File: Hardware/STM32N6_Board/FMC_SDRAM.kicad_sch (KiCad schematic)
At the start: 15 parts, among them U11 IS42S16800F-7BL

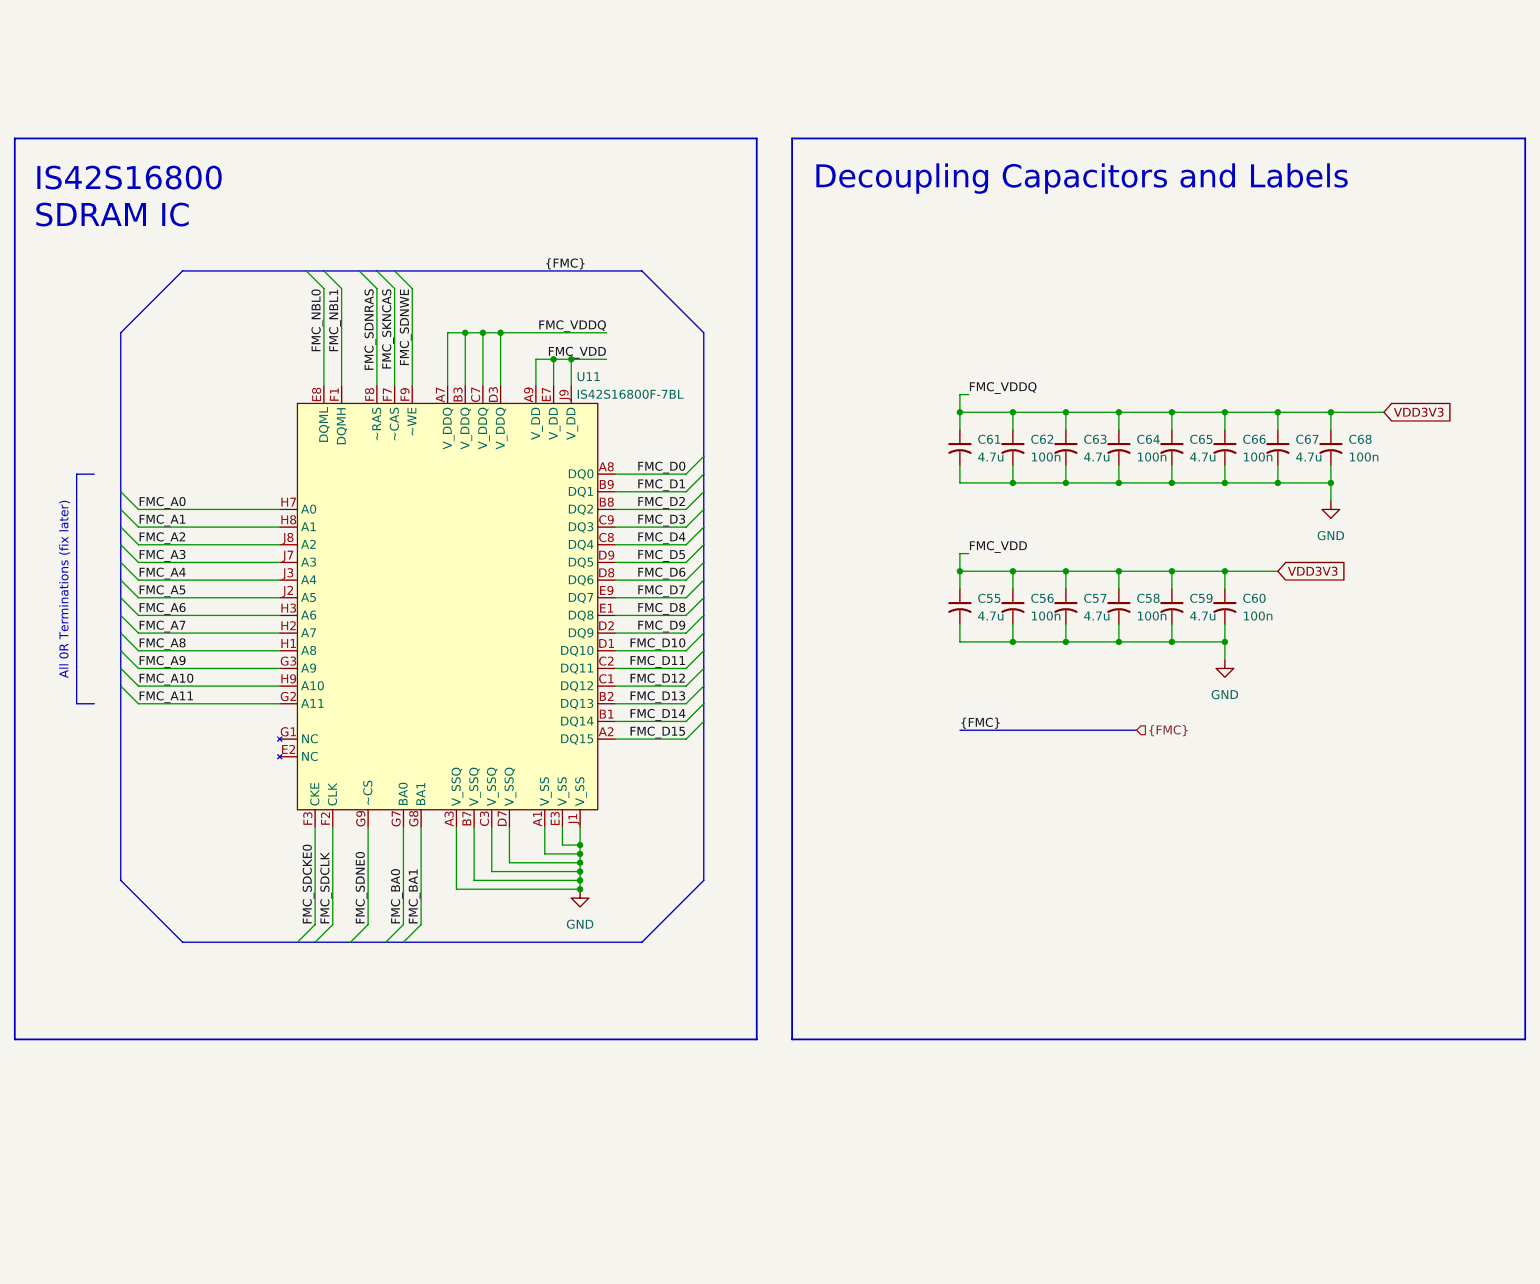
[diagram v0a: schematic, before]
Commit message: Completed the IS42S SDRAM routing. Lord have mercy
- Routing is complete (somewhat)
- Spacing between traces is 0.5mm, address and data lines 0.1565mm wide
- 0.1565mm should maintain ~50 Ohms impedance.
- STILL NEED TO DO:
  - Length matching. Datasheet + STM App Note says +-10mm
  - 10nF stitching caps along vias, for return currents
- Remind me to *never* use a 4-layer board for something like this
  again. D:
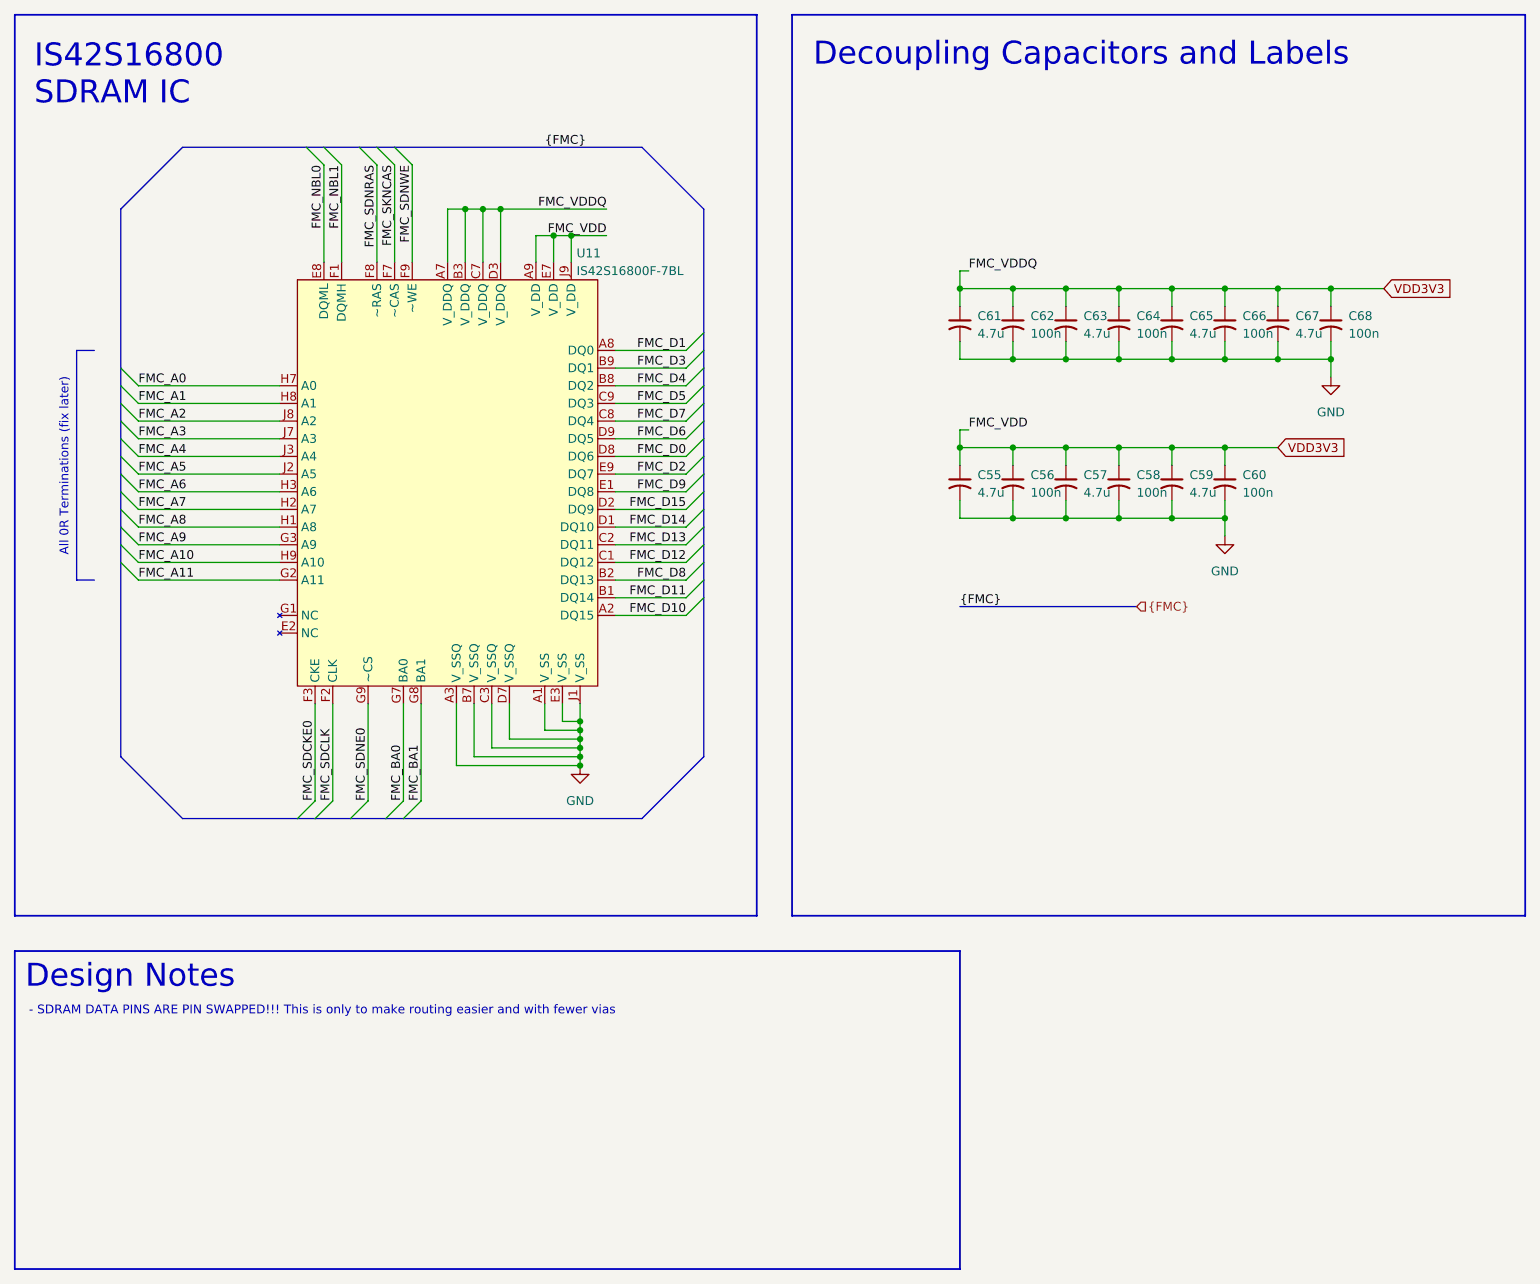
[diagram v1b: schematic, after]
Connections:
- net FMC_D0: now also U11.D8 (DQ6); no longer U11.A8 (DQ0)
- net FMC_D1: now also U11.A8 (DQ0); no longer U11.B9 (DQ1)
- net FMC_D10: now also U11.A2 (DQ15); no longer U11.D1 (DQ10)
- net FMC_D11: now also U11.B1 (DQ14); no longer U11.C2 (DQ11)
- net FMC_D13: now also U11.C2 (DQ11); no longer U11.B2 (DQ13)
- net FMC_D14: now also U11.D1 (DQ10); no longer U11.B1 (DQ14)
- net FMC_D15: now also U11.D2 (DQ9); no longer U11.A2 (DQ15)
- net FMC_D2: now also U11.E9 (DQ7); no longer U11.B8 (DQ2)
- net FMC_D3: now also U11.B9 (DQ1); no longer U11.C9 (DQ3)
- net FMC_D4: now also U11.B8 (DQ2); no longer U11.C8 (DQ4)
- net FMC_D5: now also U11.C9 (DQ3); no longer U11.D9 (DQ5)
- net FMC_D6: now also U11.D9 (DQ5); no longer U11.D8 (DQ6)
- net FMC_D7: now also U11.C8 (DQ4); no longer U11.E9 (DQ7)
- net FMC_D8: now also U11.B2 (DQ13); no longer U11.E1 (DQ8)
- net FMC_D9: now also U11.E1 (DQ8); no longer U11.D2 (DQ9)
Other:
- note added: "- SDRAM DATA PINS ARE PIN SWAPPED!!! This is only to make routing easier and with fewer vias"
- note added: "Design Notes"
- moved on the sheet: C55, C56, C57, C58, C59, C60, C61, C62, C63, C64, C65, C66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

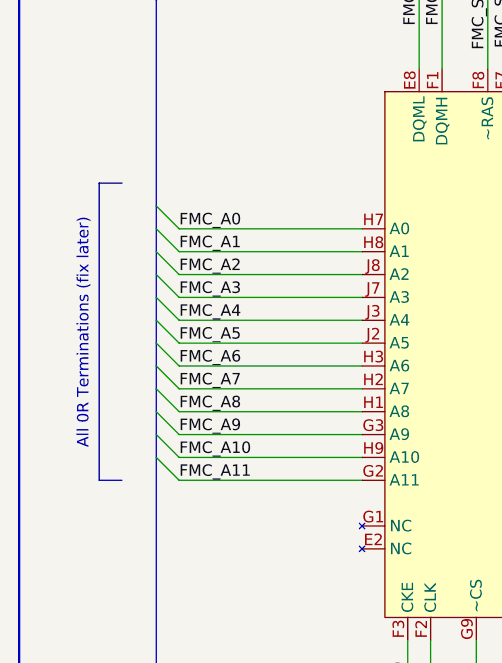
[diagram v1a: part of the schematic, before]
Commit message: Updated the schematic with latest changes
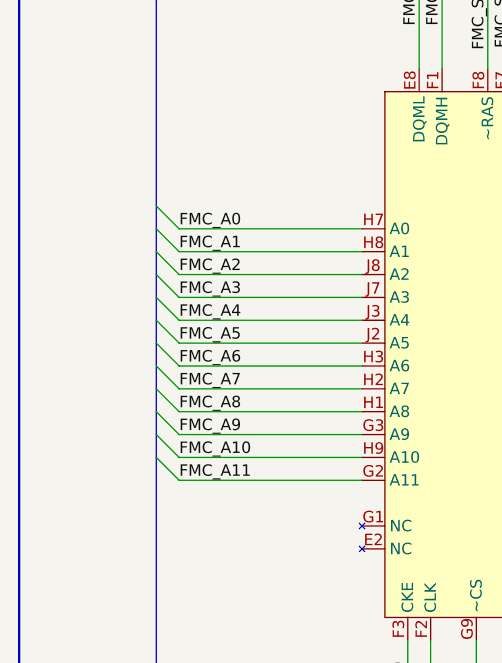
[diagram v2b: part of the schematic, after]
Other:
- note removed: "All 0R Terminations (fix later)"
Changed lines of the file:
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@@
-		)
-	)
-	(text "All 0R Terminations (fix later)"
-		(exclude_from_sim no)
-		(at 46.482 80.264 90)
-		(effects
-			(font
-				(size 1.27 1.27)
-			)
 		)
 	)
@@
 		)
 	)
-	(polyline
-		(pts
-			(xy 50.8 63.5) (xy 48.26 63.5)
-		)
-		(stroke
-			(width 0)
-			(type default)
-		)
-	)
 	(bus
 		(pts
@@
 		)
 	)
-	(polyline
-		(pts
-			(xy 48.26 63.5) (xy 48.26 96.52)
-		)
-		(stroke
-			(width 0)
-			(type default)
-		)
-	)
 	(wire
 		(pts
@@
 		)
 		(stroke
-			(width 0)
-			(type default)
-		)
-	)
-	(polyline
-		(pts
-			(xy 48.26 96.52) (xy 50.8 96.52)
-		)
-		(stroke
